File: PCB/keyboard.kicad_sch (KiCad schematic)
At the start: 153 parts, among them J1 JST SH 4-pin, SW1 SW_Push, U1 ATmega32U4-A, U2 SRV05-4, Y1 16MHz

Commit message: Working on traces
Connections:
- net D + is gone; now on net D+: R1.1
- net D - is gone; now on net D-: R2.1
- net COL0: now also U1.18 (PD0)
- net COL1: now also U1.11 (PB3)
- net COL10: now also U1.41 (PF0)
- net COL11: now also U1.1 (PE6)
- net COL12: now also U1.12 (PB7)
- net COL13: now also U1.22 (PD5)
- net COL14: now also U1.21 (PD3)
- net COL2: now also U1.10 (PB2)
- net COL3: now also U1.9 (PB1)
- net COL4: now also U1.8 (PB0)
- net COL5: now also U1.36 (PF7)
- net COL6: now also U1.37 (PF6)
- net COL7: now also U1.38 (PF5)
- net COL8: now also U1.39 (PF4)
- net COL9: now also U1.40 (PF1)
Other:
- moved on the sheet: U2

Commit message: finnished traces
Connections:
- net ROW0: now also U1.25 (PD4)
- net ROW1: now also U1.26 (PD6)
- net ROW2: now also U1.27 (PD7)
- net ROW3: now also U1.28 (PB4)
- net ROW4: now also U1.29 (PB5)
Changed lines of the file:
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@@
+    )
+  )
+  (global_label "ROW1" (shape input) (at 373.38 80.01 0) (fields_autoplaced)
+    (effects (font (size 1.27 1.27)) (justify left))
+    (property "Intersheetrefs" "${INTERSHEET_REFS}" (id 0) (at 380.988 80.01 0)
+      (effects (font (size 1.27 1.27)) (justify left) hide)
     )
   )
@@
     (effects (font (size 1.27 1.27)) (justify left))
     (property "Intersheetrefs" "${INTERSHEET_REFS}" (id 0) (at 106.68 126.1653 90)
+      (effects (font (size 1.27 1.27)) (justify left) hide)
+    )
+  )
+  (global_label "ROW0" (shape input) (at 373.38 74.93 0) (fields_autoplaced)
+    (effects (font (size 1.27 1.27)) (justify left))
+    (property "Intersheetrefs" "${INTERSHEET_REFS}" (id 0) (at 380.988 74.93 0)
       (effects (font (size 1.27 1.27)) (justify left) hide)
     )
@@
     )
   )
+  (global_label "ROW2" (shape input) (at 373.38 82.55 0) (fields_autoplaced)
+    (effects (font (size 1.27 1.27)) (justify left))
+    (property "Intersheetrefs" "${INTERSHEET_REFS}" (id 0) (at 380.988 82.55 0)
+      (effects (font (size 1.27 1.27)) (justify left) hide)
+    )
+  )
   (global_label "COL7" (shape input) (at 373.38 102.87 0) (fields_autoplaced)
     (effects (font (size 1.27 1.27)) (justify left))
@@
     )
   )
+  (global_label "ROW4" (shape input) (at 373.38 46.99 0) (fields_autoplaced)
+    (effects (font (size 1.27 1.27)) (justify left))
+    (property "Intersheetrefs" "${INTERSHEET_REFS}" (id 0) (at 380.988 46.99 0)
+      (effects (font (size 1.27 1.27)) (justify left) hide)
+    )
+  )
   (global_label "COL10" (shape input) (at 373.38 95.25 0) (fields_autoplaced)
     (effects (font (size 1.27 1.27)) (justify left))
@@
       (effects (font (size 1.27 1.27)) (justify left) hide)
     )
+  )
+  (global_label "ROW3" (shape input) (at 373.38 44.45 0) (fields_autoplaced)
+    (effects (font (size 1.27 1.27)) (justify left))
+    (property "Intersheetrefs" "${INTERSHEET_REFS}" (id 0) (at 380.988 44.45 0)
+      (effects (font (size 1.27 1.27)) (justify left) hide)
+    )

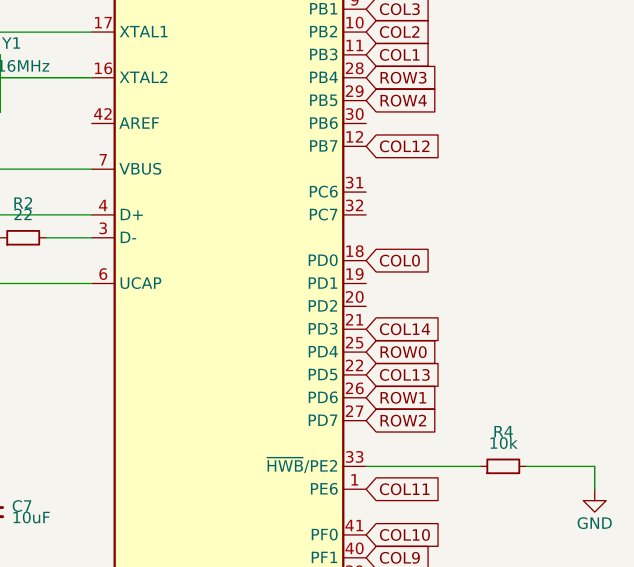
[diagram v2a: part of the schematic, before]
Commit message: started redoing wiring
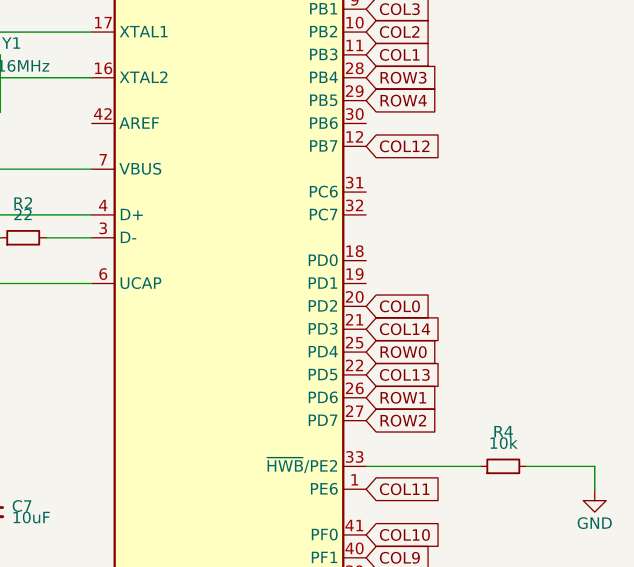
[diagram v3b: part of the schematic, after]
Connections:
- net COL0: now also U1.20 (PD2); no longer U1.18 (PD0)
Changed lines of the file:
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@@
     )
   )
-  (global_label "COL0" (shape input) (at 373.38 64.77 0) (fields_autoplaced)
+  (global_label "COL0" (shape input) (at 373.38 69.85 0) (fields_autoplaced)
     (effects (font (size 1.27 1.27)) (justify left))
-    (property "Intersheetrefs" "${INTERSHEET_REFS}" (id 0) (at 380.5647 64.77 0)
+    (property "Intersheetrefs" "${INTERSHEET_REFS}" (id 0) (at 380.5647 69.85 0)
       (effects (font (size 1.27 1.27)) (justify left) hide)
     )

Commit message: all new pretty wiring
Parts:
- removed D20, D25, D8, D9: D_Small, Diode_SMD:D_SOD-123, symbol Device:D_Small
- added D35, D50, D65, D66: D_Small, Diode_SMD:D_SOD-123, symbol Device:D_Small
- renumbered D18 to D13, D19 to D14, D23 to D18, D24 to D19, D35 to D20, D28 to D23, D29 to D24, D50 to D25, D33 to D28, D34 to D29, D38 to D33, D39 to D34, D43 to D38, D44 to D39, D48 to D43, D49 to D44, D53 to D48, D54 to D49, D57 to D53, D58 to D54, D61 to D57, D62 to D58, D65 to D61, D66 to D62, D13 to D8, D14 to D9
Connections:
- net COL0: now also U1.25 (PD4); no longer U1.20 (PD2)
- net COL1: now also U1.26 (PD6); no longer MX8.1 (COL), MX9.1 (COL), U1.11 (PB3)
- net COL10: now also MX30.1 (COL), MX48.1 (COL), MX49.1 (COL), U1.38 (PF5); no longer MX53.1 (COL), MX54.1 (COL), U1.41 (PF0)
- net COL11: now also MX35.1 (COL), MX53.1 (COL), MX54.1 (COL), U1.39 (PF4); no longer MX57.1 (COL), MX58.1 (COL), U1.1 (PE6)
- net COL12: now also MX40.1 (COL), MX57.1 (COL), MX58.1 (COL), U1.40 (PF1); no longer MX61.1 (COL), MX62.1 (COL), U1.12 (PB7)
- net COL13: now also MX45.1 (COL), MX61.1 (COL), MX62.1 (COL), U1.41 (PF0); no longer MX65.1 (COL), MX66.1 (COL), U1.22 (PD5)
- net COL14: now also MX50.1 (COL), MX65.1 (COL), MX66.1 (COL), U1.12 (PB7); no longer U1.21 (PD3)
- net COL2: now also MX8.1 (COL), MX9.1 (COL), U1.27 (PD7); no longer MX13.1 (COL), MX14.1 (COL), U1.10 (PB2)
- net COL3: now also MX13.1 (COL), MX14.1 (COL), U1.28 (PB4); no longer MX18.1 (COL), MX19.1 (COL), MX20.1 (COL), U1.9 (PB1)
- net COL4: now also MX18.1 (COL), MX19.1 (COL), U1.29 (PB5); no longer MX23.1 (COL), MX24.1 (COL), MX25.1 (COL), U1.8 (PB0)
- net COL5: now also MX23.1 (COL), MX24.1 (COL), U1.30 (PB6); no longer MX28.1 (COL), MX29.1 (COL), MX30.1 (COL), U1.36 (PF7)
- net COL6: now also MX20.1 (COL), MX28.1 (COL), MX29.1 (COL), U1.31 (PC6); no longer MX33.1 (COL), MX34.1 (COL), MX35.1 (COL), U1.37 (PF6)
- net COL7: now also MX33.1 (COL), MX34.1 (COL), U1.32 (PC7); no longer MX38.1 (COL), MX39.1 (COL), MX40.1 (COL), U1.38 (PF5)
- net COL8: now also MX38.1 (COL), MX39.1 (COL), U1.36 (PF7); no longer MX43.1 (COL), MX44.1 (COL), MX45.1 (COL), U1.39 (PF4)
- net COL9: now also MX25.1 (COL), MX43.1 (COL), MX44.1 (COL), U1.37 (PF6); no longer MX48.1 (COL), MX49.1 (COL), MX50.1 (COL), U1.40 (PF1)
- net ROW0: now also U1.1 (PE6); no longer U1.25 (PD4)
- net ROW1: now also U1.11 (PB3); no longer U1.26 (PD6)
- net ROW2: now also U1.10 (PB2), D65.1 (K); no longer U1.27 (PD7)
- net ROW3: now also U1.9 (PB1), D66.1 (K); no longer U1.28 (PB4)
- net ROW4: now also U1.8 (PB0), D35.1 (K), D50.1 (K); no longer U1.29 (PB5)
- net at MX34.2 (ROW): now also D34.2 (A); no longer D29.2 (A)
- net at MX48.2 (ROW): now also D48.2 (A); no longer D43.2 (A)
- net at MX20.2 (ROW): now also D20.2 (A)
- net at MX35.2 (ROW): now also D35.2 (A); no longer D20.2 (A)
- net at MX39.2 (ROW): now also D39.2 (A); no longer D34.2 (A)
- net at MX61.2 (ROW): now also D61.2 (A); no longer D57.2 (A)
- net at D8.2 (A): now also MX8.2 (ROW); no longer MX13.2 (ROW)
- net at D54.2 (A): now also MX54.2 (ROW); no longer MX58.2 (ROW)
- net at MX57.2 (ROW): now also D57.2 (A); no longer D53.2 (A)
- net at D58.2 (A): now also MX58.2 (ROW); no longer MX62.2 (ROW)
- net at D13.2 (A): now also MX13.2 (ROW); no longer MX18.2 (ROW)
- net at MX65.2 (ROW): now also D65.2 (A); no longer D61.2 (A)
- net at MX49.2 (ROW): now also D49.2 (A); no longer D44.2 (A)
- net at MX9.2 (ROW): now also D9.2 (A)
- net at MX14.2 (ROW): now also D14.2 (A); no longer D9.2 (A)
- net at MX33.2 (ROW): now also D33.2 (A); no longer D28.2 (A)
- net at MX38.2 (ROW): now also D38.2 (A); no longer D33.2 (A)
- net at MX23.2 (ROW): now also D23.2 (A); no longer D18.2 (A)
- net at MX25.2 (ROW): now also D25.2 (A)
- net at MX19.2 (ROW): now also D19.2 (A); no longer D14.2 (A)
- net at MX28.2 (ROW): now also D28.2 (A); no longer D23.2 (A)
- net at MX50.2 (ROW): now also D50.2 (A); no longer D25.2 (A)
- net at MX24.2 (ROW): now also D24.2 (A); no longer D19.2 (A)
- net at MX43.2 (ROW): now also D43.2 (A); no longer D38.2 (A)
- net at D62.2 (A): now also MX62.2 (ROW); no longer MX66.2 (ROW)
- net at MX44.2 (ROW): now also D44.2 (A); no longer D39.2 (A)
- net at MX53.2 (ROW): now also D53.2 (A); no longer D48.2 (A)
- net at MX29.2 (ROW): now also D29.2 (A); no longer D24.2 (A)
- new net: D18.2 (A), MX18.2 (ROW)
- new net: D66.2 (A), MX66.2 (ROW)
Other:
- moved on the sheet: MX13, MX14, MX18, MX19, MX20, MX23, MX24, MX25, MX28, MX29, MX30, MX33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

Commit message: Redid wiring again
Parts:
- U2: footprint Package_TO_SOT_SMD:SOT-23-6 -> marbastlib-various:SOT-23-6-routable
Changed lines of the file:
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@@
       (effects (font (size 1.27 1.27)))
     )
-    (property "Footprint" "Package_TO_SOT_SMD:SOT-23-6" (id 2) (at 223.52 50.8 0)
+    (property "Footprint" "marbastlib-various:SOT-23-6-routable" (id 2) (at 223.52 50.8 0)
       (effects (font (size 1.27 1.27)) hide)
     )
@@
     )
     (path "/ef12052d-f84d-46d8-a991-3451abdfdbc0"
-      (reference "U2") (unit 1) (value "SRV05-4") (footprint "Package_TO_SOT_SMD:SOT-23-6")
+      (reference "U2") (unit 1) (value "SRV05-4") (footprint "marbastlib-various:SOT-23-6-routable")
     )
     (path "/554c564d-e286-4b2b-aa94-325d745117a1"
